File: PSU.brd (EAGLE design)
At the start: 840 x 60 mm, 40 parts, among them IC1 7812T, IC2 LM7912, Q1 TIP120, Q2 TIP125, X1 332-16, X10 332-16, X11 332-16, X12 332-16, X13 332-16, X14 332-16, X2 332-16, X3 332-16, X4 332-16, X5 332-16, X6 332-16, X7 332-16, X8 332-16, X9 332-16

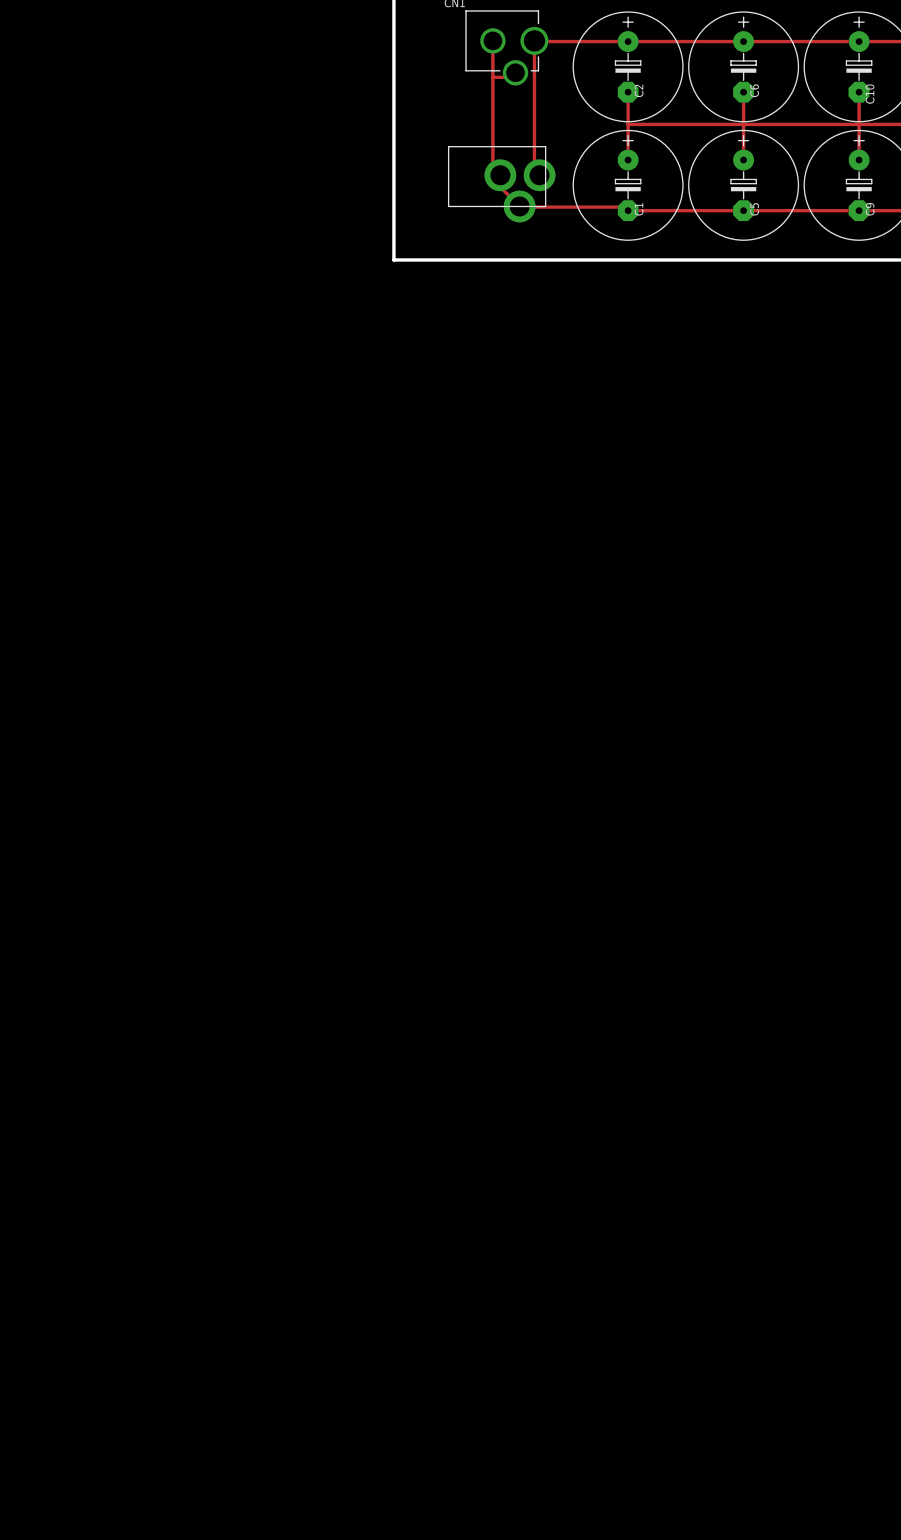
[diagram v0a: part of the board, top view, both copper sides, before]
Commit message: A different approach
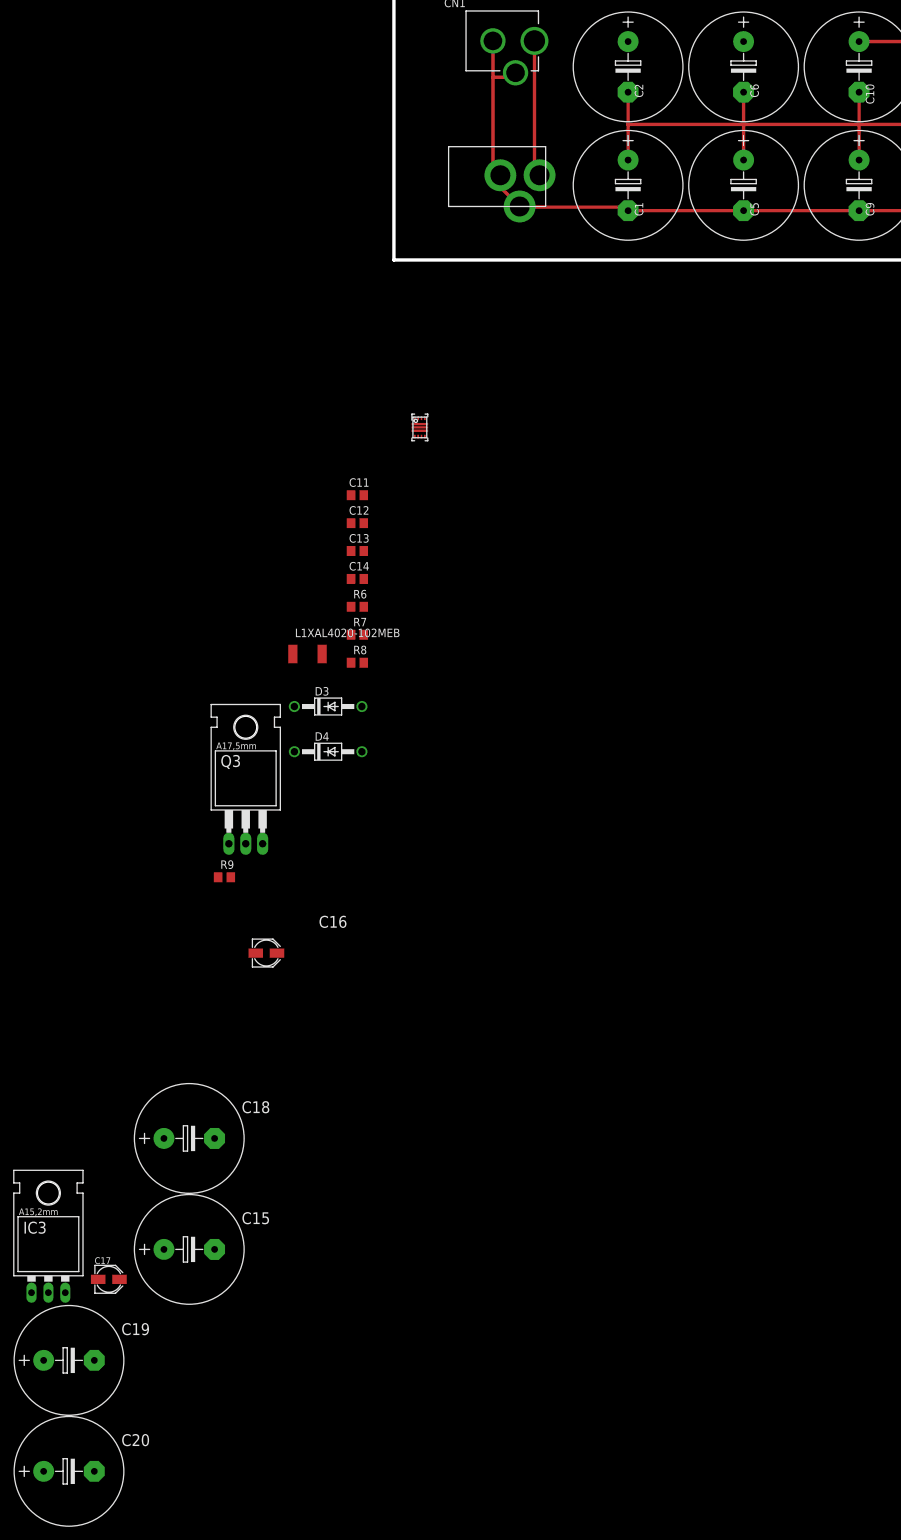
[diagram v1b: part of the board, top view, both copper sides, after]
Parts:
- added C11: 2.2nF, rcl:C0805
- added C12: 6.8uF, rcl:C0805
- added C13, C14: 4.7uF, rcl:C0805
- added C15: 100uF, rcl:E7,5-16
- added C16, C17: 10uF, rcl:PANASONIC_B
- added C18: 2200uF, rcl:E7,5-16
- added C19: 1uF, rcl:E7,5-16
- added C20: 2.2uF, rcl:E7,5-16
- added D3, D4: 1N4004, diode:DO41-10
- added IC3: LM7912, v-reg:79XXL
- added L1XAL4020-102MEB: 1uH, rcl:L5038P
- added Q3: TIP125, transistor-power:TO220AH
- added R6: 1.62M, rcl:R0805
- added R7, R8: 100k, rcl:R0805
- added R9: 1k, rcl:R0805
- added U2: Value, texas12vsupply:RGX0011A
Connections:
- removed net +24V: C10.+, C2.+, C3.1, C6.+, CN1.PWR, IC1.1, U$1.TIP
- removed net GNDA: C1.-, C4.2, C5.-, C9.-, CN1.GND, CN1.GNDBREAK, IC2.IN, U$1.RING, U$1.RING_SW
- new net +15V: C12.1, CN1.PWR, U$1.TIP, U2.1
- new net 10: U2.8
- new net 14P4: C17.+, L1XAL4020-102MEB.1, U2.2
- new net N$1: R8.2, U2.7
- new net N$10: C11.1, U2.9
- new net N$11: R6.1, R7.2, U2.5
- new net N$12: C16.-, Q3.B, R9.1
- new net N$13: C17.-, D3.A, D4.C
- new net N$3: C15.-, C18.-, C20.-, D4.A, IC3.IN
- new net N$7: C10.+, C2.+, C3.1, C6.+, IC1.1
- new net N$8: C1.-, C4.2, C5.-, C9.-, IC2.IN
- new net N$9: C19.-, IC3.OUT, Q3.C, R9.2
- net +12V: now also C13.1, C14.1, L1XAL4020-102MEB.2, R6.2, R8.1, U2.6
- net -12V: now also Q3.E
- net GND: now also C11.2, C12.2, C13.2, C14.2, C15.+, C16.+, C18.+, C19.+, C20.+, CN1.GND, CN1.GNDBREAK, D3.C, IC3.GND, R7.1, U$1.RING, U$1.RING_SW, U2.10, U2.11, U2.3, U2.4
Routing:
- net GNDA: track 102.8 -> 0.00 mm
- net +24V: track 89.6 -> 0.00 mm
- net N$8: track 0.00 -> 55.9 mm
- net GND: track 2200.4 -> 2246.5 mm
- net +15V: track 0.00 -> 21.3 mm
- net N$7: track 0.00 -> 19.5 mm

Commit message: Update
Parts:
- removed C1, C10, C18, C2, C5, C6, C9: 2200uF, rcl:E7,5-16
- removed C3, C4: 22uF, rcl:C025-025X050
- removed C7, C8: 10uF, rcl:C025-025X050
- removed D1, D2: 1N4004, diode:DO41-10
- removed IC1: 7812T, linear:TO220H
- removed IC2: LM7912, v-reg:79XXL
- removed Q1: TIP120, transistor-power:TO220AH
- removed Q2, Q3: TIP125, transistor-power:TO220AH
- removed R1, R2: 1k, rcl:0207/7
- removed X10, X11, X12, X13, X14, X9: 332-16, con-garry:332-16
- added U$2: MPS751, audioic:TO92-EBC
- C15, C19, C20: device rcl:E7,5-16 -> rcl:PANASONIC_B
- C16: value 10uF -> 100uF
- moved C20 222.8 mm to (45.0, 19.8), turned to 90 degrees
- moved C19 216.2 mm to (51.2, 26.0), turned to 180 degrees
- moved IC3 200.0 mm to (53.6, 18.2), turned to 270 degrees
- moved C17 186.5 mm to (27.1, 19.5), turned to 90 degrees
- moved C15 183.1 mm to (40.4, 19.8), turned to 90 degrees
- moved C16 153.6 mm to (56.1, 29.6), turned to 180 degrees
- moved LED1 146.4 mm to (16.4, 44.0), turned to 90 degrees
- moved R9 144.3 mm to (56.4, 25.9), turned to 180 degrees
- moved LED2 141.6 mm to (23.2, 43.3)
- moved X8 129.1 mm to (393.9, 23.4)
- moved X7 126.1 mm to (346.8, 23.4)
- moved R5 125.4 mm to (32.2, 34.7), turned to 90 degrees
- moved X6 119.6 mm to (303.2, 23.4)
- moved R4 116.6 mm to (38.3, 33.3), turned to 90 degrees
- moved LED3 116.4 mm to (30.1, 44.0), turned to 90 degrees
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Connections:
- removed net N$2: IC2.OUT, Q2.E, R2.1
- removed net N$4: IC1.3, Q1.C, R1.1
- removed net N$5: C7.1, Q1.B, R1.2
- removed net N$6: C8.2, Q2.B, R2.2
- removed net N$7: C10.+, C2.+, C3.1, C6.+, IC1.1
- removed net N$8: C1.-, C4.2, C5.-, C9.-, IC2.IN
- net +12V: no longer D1.C, Q1.E, X10.10, X10.9, X11.10, X11.9, X12.10, X12.9, X13.10, X13.9, X14.10, X14.9, X9.10, X9.9
- net +5V: no longer X10.11, X10.12, X11.11, X11.12, X12.11, X12.12, X13.11, X13.12, X14.11, X14.12, X9.11, X9.12
- net -12V: now also U$2.E; no longer D2.A, Q2.C, Q3.E, X10.1, X10.2, X11.1, X11.2, X12.1, X12.2, X13.1, X13.2, X14.1, X14.2, X9.1, X9.2
- net GND: no longer C1.+, C10.-, C18.+, C2.-, C3.2, C4.1, C5.+, C6.-, C7.2, C8.1, C9.+, D1.A, D2.C, IC1.2, IC2.GND, X10.3, X10.4, X10.5, X10.6, X10.7, X10.8, X11.3, X11.4, X11.5, X11.6, X11.7, X11.8, X12.3, X12.4, X12.5, X12.6, X12.7, X12.8, X13.3, X13.4, X13.5, X13.6, X13.7, X13.8, X14.3, X14.4, X14.5, X14.6, X14.7, X14.8, X9.3, X9.4, X9.5, X9.6, X9.7, X9.8
- net N$12: now also U$2.B; no longer Q3.B
- net N$19: no longer X10.15, X10.16, X11.15, X11.16, X12.15, X12.16, X13.15, X13.16, X14.15, X14.16, X9.15, X9.16
- net N$20: no longer X10.13, X10.14, X11.13, X11.14, X12.13, X12.14, X13.13, X13.14, X14.13, X14.14, X9.13, X9.14
- net N$3: no longer C18.-
- net N$9: now also U$2.C; no longer Q3.C
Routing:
- net GND: track 2246.5 -> 1142.4 mm
- net -12V: track 707.1 -> 363.0 mm
- net N$20: track 654.0 -> 310.9 mm
- net N$19: track 654.0 -> 311.6 mm
- net +12V: track 699.1 -> 389.5 mm
- net +5V: track 654.0 -> 350.4 mm
- net N$2: track 70.2 -> 0.00 mm
- net N$4: track 58.3 -> 0.00 mm
- net N$8: track 55.9 -> 0.00 mm
- net N$9: track 0.00 -> 22.9 mm
- net N$7: track 19.5 -> 0.00 mm
- net N$3: track 0.00 -> 18.6 mm
- net N$5: track 16.8 -> 0.00 mm
- net N$11: track 0.00 -> 15.0 mm
- net N$14: track 4.08 -> 17.5 mm
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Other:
- board size 840 x 60 mm -> 400 x 60 mm
- board text added: "GATE CV +5V +12V GND GND GND -12V"
- board text added: "GATE CV +5V +12V GND GND GND -12V [RED STRIPE]_"

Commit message: layout update
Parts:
- moved C11 0.40 mm to (22.0, 20.7)
- moved R7 0.20 mm to (34.5, 27.3)
- moved C13 0.20 mm to (32.4, 27.3)
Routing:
- net GND: track 1142.4 -> 48.9 mm
- net -12V: track 363.0 -> 364.4 mm
- net +12V: track 389.5 -> 390.8 mm
- net N$19: track 311.6 -> 310.9 mm
- added copper zone on layer 1, net GND
